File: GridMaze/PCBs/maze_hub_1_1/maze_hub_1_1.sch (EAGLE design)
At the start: 29 parts, among them IC1 7805DT, IC2 TBD62083, IC3 PCA9517D, IC4 PCA9517D, IC5 MCP4541-104E/MS, IC6 OPA197

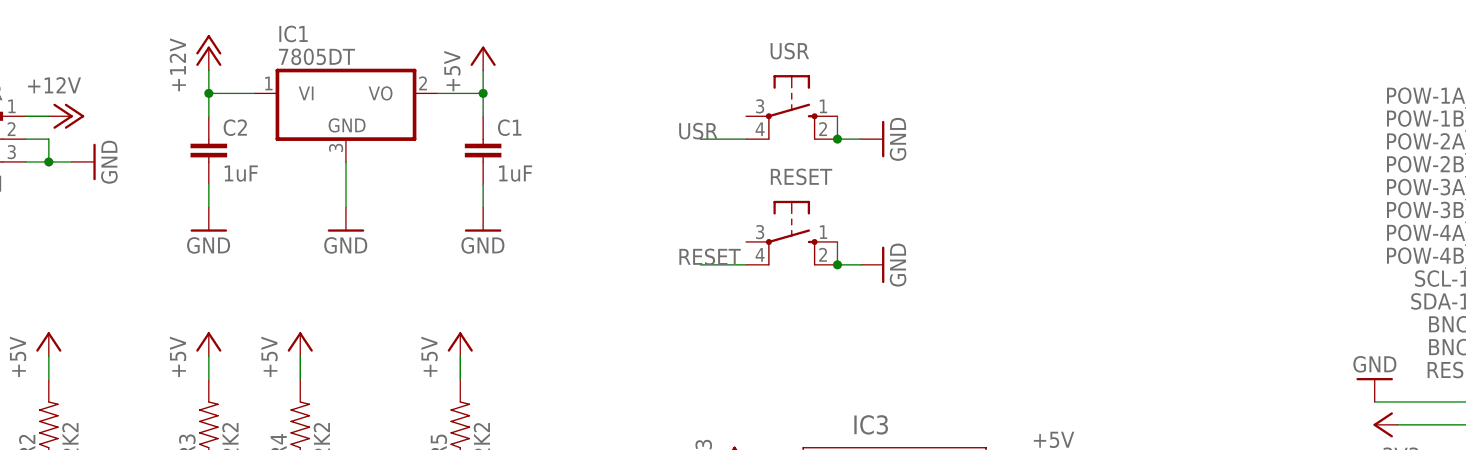
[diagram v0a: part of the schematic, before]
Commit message: Changes to 3x3 GridMaze hardware:
- Rather than seperate tall and short variants there is now a single intermediate height version of the maze.

- IR illumination is now provided by IR module PCBs which connect to the maze hub board using a Molex Micro-Fit cable and can be daisy chained.

- Reduced Poke IR beam current from 50mA to 40mA.
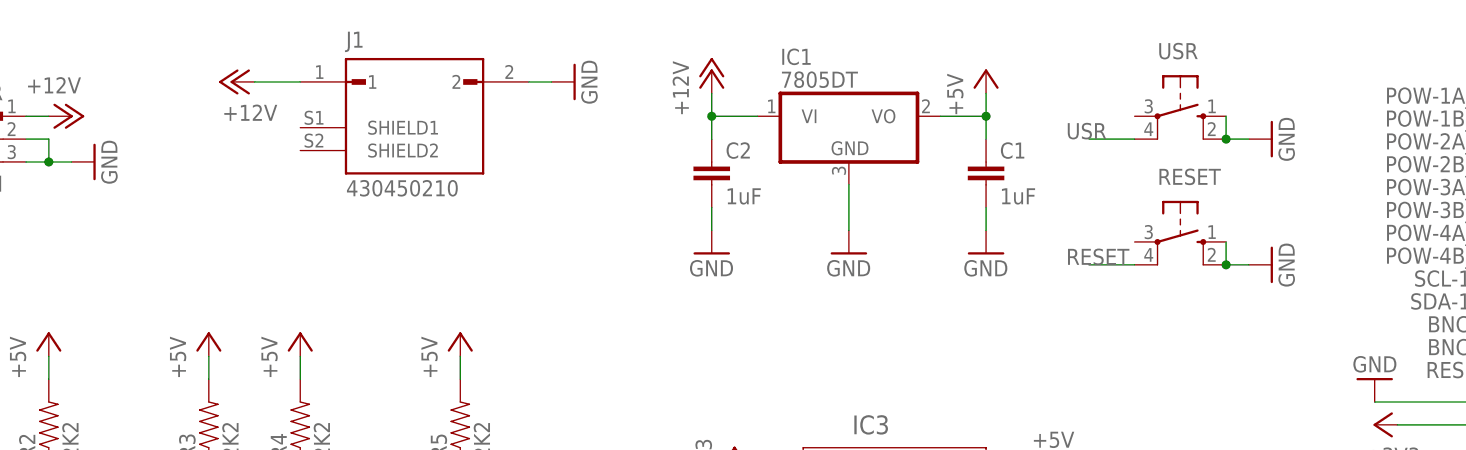
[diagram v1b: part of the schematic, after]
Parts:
- added J1: 430450210, Molex_430450210:430450210
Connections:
- net +12V: now also J1.1
- net GND: now also J1.2
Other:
- moved on the sheet: C1, C2, IC1, RESET, USR
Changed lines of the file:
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@@
 <part name="P+23" library="supply1" deviceset="+5V" device=""/>
 <part name="IC5" library="Digital_potentiometers" deviceset="MCP4541-104E/MS" device=""/>
+<part name="J1" library="Molex_430450210" deviceset="430450210" device=""/>
+<part name="GND13" library="supply1" deviceset="GND" device=""/>
+<part name="P+24" library="supply1" deviceset="+12V" device=""/>
 </parts>
 <sheets>
@@
 </plain>
 <instances>
-<instance part="GND37" gate="1" x="82.55" y="140.97" rot="R90"/>
-<instance part="GND17" gate="1" x="82.55" y="127" rot="R90"/>
+<instance part="GND37" gate="1" x="125.73" y="140.97" rot="R90"/>
+<instance part="GND17" gate="1" x="125.73" y="127" rot="R90"/>
 <instance part="BNC-1" gate="G$1" x="-11.43" y="44.45"/>
 <instance part="BNC-2" gate="G$1" x="-11.43" y="31.75"/>
-<instance part="RESET" gate="1" x="72.39" y="129.54" rot="R270"/>
+<instance part="RESET" gate="1" x="115.57" y="129.54" rot="R270"/>
 <instance part="GND62" gate="1" x="1.27" y="41.91" rot="R90"/>
 <instance part="GND63" gate="1" x="1.27" y="29.21" rot="R90"/>
-<instance part="C1" gate="G$1" x="38.1" y="140.97"/>
-<instance part="C2" gate="G$1" x="7.62" y="140.97"/>
-<instance part="P+2" gate="1" x="7.62" y="151.13"/>
-<instance part="GND2" gate="1" x="7.62" y="130.81"/>
-<instance part="GND3" gate="1" x="22.86" y="130.81"/>
-<instance part="GND4" gate="1" x="38.1" y="130.81"/>
+<instance part="C1" gate="G$1" x="93.98" y="138.43"/>
+<instance part="C2" gate="G$1" x="63.5" y="138.43"/>
+<instance part="P+2" gate="1" x="63.5" y="148.59"/>
+<instance part="GND2" gate="1" x="63.5" y="128.27"/>
+<instance part="GND3" gate="1" x="78.74" y="128.27"/>
+<instance part="GND4" gate="1" x="93.98" y="128.27"/>
 <instance part="GND72" gate="1" x="-10.16" y="63.5" rot="R270"/>
 <instance part="PORT-1" gate="G$1" x="5.08" y="5.08"/>
@@
 <instance part="P+14" gate="1" x="86.36" y="-5.08" rot="R90"/>
 <instance part="P+15" gate="1" x="86.36" y="2.54"/>
-<instance part="P+10" gate="1" x="38.1" y="151.13"/>
+<instance part="P+10" gate="1" x="93.98" y="148.59"/>
 <instance part="POW_CON" gate="G$1" x="-17.78" y="140.97" rot="R180"/>
 <instance part="GND15" gate="1" x="-5.08" y="138.43" rot="R90"/>
@@
 <instance part="GND8" gate="1" x="137.16" y="114.3" rot="R180"/>
 <instance part="FRAME1" gate="G$1" x="-35.56" y="-17.78"/>
-<instance part="USR" gate="1" x="72.39" y="143.51" rot="R270"/>
-<instance part="IC1" gate="A1" x="22.86" y="146.05"/>
+<instance part="USR" gate="1" x="115.57" y="143.51" rot="R270"/>
+<instance part="IC1" gate="A1" x="78.74" y="143.51"/>
 <instance part="SV1" gate="G$1" x="35.56" y="40.64" rot="R180"/>
 <instance part="P+4" gate="1" x="22.86" y="30.48" rot="R90"/>
@@
 <instance part="P+23" gate="1" x="35.56" y="119.38"/>
 <instance part="IC5" gate="G$1" x="134.62" y="43.18"/>
+<instance part="J1" gate="G$1" x="30.48" y="144.78"/>
+<instance part="GND13" gate="1" x="48.26" y="147.32" rot="R90"/>
+<instance part="P+24" gate="1" x="10.16" y="147.32" rot="R90"/>
 </instances>
 <busses>
@@
 <segment>
 <pinref part="P+2" gate="1" pin="+12V"/>
-<wire x1="12.7" y1="146.05" x2="7.62" y2="146.05" width="0.1524" layer="91"/>
-<wire x1="7.62" y1="146.05" x2="7.62" y2="148.59" width="0.1524" layer="91"/>
+<wire x1="68.58" y1="143.51" x2="63.5" y2="143.51" width="0.1524" layer="91"/>
+<wire x1="63.5" y1="143.51" x2="63.5" y2="146.05" width="0.1524" layer="91"/>
 <pinref part="C2" gate="G$1" pin="1"/>
-<wire x1="7.62" y1="143.51" x2="7.62" y2="146.05" width="0.1524" layer="91"/>
-<junction x="7.62" y="146.05"/>
+<wire x1="63.5" y1="140.97" x2="63.5" y2="143.51" width="0.1524" layer="91"/>
+<junction x="63.5" y="143.51"/>
 <pinref part="IC1" gate="A1" pin="VI"/>
 </segment>
@@
 <wire x1="27.178" y1="61.722" x2="22.86" y2="66.04" width="0.1524" layer="91"/>
 </segment>
+<segment>
+<pinref part="J1" gate="G$1" pin="1"/>
+<pinref part="P+24" gate="1" pin="+12V"/>
+<wire x1="12.7" y1="147.32" x2="17.78" y2="147.32" width="0.1524" layer="91"/>
+</segment>
 </net>
 <net name="GND" class="0">
 <segment>
 <pinref part="GND37" gate="1" pin="GND"/>
-<wire x1="77.47" y1="140.97" x2="80.01" y2="140.97" width="0.1524" layer="91"/>
-<wire x1="77.47" y1="143.51" x2="77.47" y2="140.97" width="0.1524" layer="91"/>
+<wire x1="120.65" y1="140.97" x2="123.19" y2="140.97" width="0.1524" layer="91"/>
+<wire x1="120.65" y1="143.51" x2="120.65" y2="140.97" width="0.1524" layer="91"/>
 <pinref part="USR" gate="1" pin="S"/>
 <pinref part="USR" gate="1" pin="S1"/>
-<junction x="77.47" y="140.97"/>
+<junction x="120.65" y="140.97"/>
 </segment>
 <segment>
 <pinref part="GND17" gate="1" pin="GND"/>
-<wire x1="77.47" y1="127" x2="80.01" y2="127" width="0.1524" layer="91"/>
+<wire x1="120.65" y1="127" x2="123.19" y2="127" width="0.1524" layer="91"/>
 <pinref part="RESET" gate="1" pin="S1"/>
 <pinref part="RESET" gate="1" pin="S"/>
-<wire x1="77.47" y1="129.54" x2="77.47" y2="127" width="0.1524" layer="91"/>
-<junction x="77.47" y="127"/>
+<wire x1="120.65" y1="129.54" x2="120.65" y2="127" width="0.1524" layer="91"/>
+<junction x="120.65" y="127"/>
 </segment>
 <segment>
@@
 <segment>
 <pinref part="GND3" gate="1" pin="GND"/>
-<wire x1="22.86" y1="133.35" x2="22.86" y2="138.43" width="0.1524" layer="91"/>
+<wire x1="78.74" y1="130.81" x2="78.74" y2="135.89" width="0.1524" layer="91"/>
 <pinref part="IC1" gate="A1" pin="GND"/>
 </segment>
@@
 <pinref part="C1" gate="G$1" pin="2"/>
 <pinref part="GND4" gate="1" pin="GND"/>
-<wire x1="38.1" y1="133.35" x2="38.1" y2="135.89" width="0.1524" layer="91"/>
+<wire x1="93.98" y1="130.81" x2="93.98" y2="133.35" width="0.1524" layer="91"/>
 </segment>
 <segment>
@@
 <pinref part="C2" gate="G$1" pin="2"/>
 <pinref part="GND2" gate="1" pin="GND"/>
-<wire x1="7.62" y1="135.89" x2="7.62" y2="133.35" width="0.1524" layer="91"/>
+<wire x1="63.5" y1="133.35" x2="63.5" y2="130.81" width="0.1524" layer="91"/>
 </segment>
 <segment>
@@
 <wire x1="66.04" y1="71.12" x2="68.58" y2="71.12" width="0.1524" layer="91"/>
 </segment>
+<segment>
+<pinref part="J1" gate="G$1" pin="2"/>
+<pinref part="GND13" gate="1" pin="GND"/>
+<wire x1="45.72" y1="147.32" x2="43.18" y2="147.32" width="0.1524" layer="91"/>
+</segment>
 </net>
 <net name="RESET" class="0">
 <segment>
-<wire x1="67.31" y1="127" x2="62.23" y2="127" width="0.1524" layer="91"/>
-<label x="59.69" y="127" size="1.778" layer="95"/>
+<wire x1="110.49" y1="127" x2="105.41" y2="127" width="0.1524" layer="91"/>
+<label x="102.87" y="127" size="1.778" layer="95"/>
 <pinref part="RESET" gate="1" pin="P1"/>
 </segment>
@@
 <segment>
 <pinref part="C1" gate="G$1" pin="1"/>
-<wire x1="38.1" y1="143.51" x2="38.1" y2="146.05" width="0.1524" layer="91"/>
-<wire x1="38.1" y1="146.05" x2="33.02" y2="146.05" width="0.1524" layer="91"/>
-<junction x="38.1" y="146.05"/>
-<wire x1="38.1" y1="146.05" x2="38.1" y2="148.59" width="0.1524" layer="91"/>
+<wire x1="93.98" y1="140.97" x2="93.98" y2="143.51" width="0.1524" layer="91"/>
+<wire x1="93.98" y1="143.51" x2="88.9" y2="143.51" width="0.1524" layer="91"/>
+<junction x="93.98" y="143.51"/>
+<wire x1="93.98" y1="143.51" x2="93.98" y2="146.05" width="0.1524" layer="91"/>
 <pinref part="P+10" gate="1" pin="+5V"/>
 <pinref part="IC1" gate="A1" pin="VO"/>
@@
 <net name="USR" class="0">
 <segment>
-<wire x1="67.31" y1="140.97" x2="62.23" y2="140.97" width="0.1524" layer="91"/>
-<label x="59.69" y="140.97" size="1.778" layer="95"/>
+<wire x1="110.49" y1="140.97" x2="105.41" y2="140.97" width="0.1524" layer="91"/>
+<label x="102.87" y="140.97" size="1.778" layer="95"/>
 <pinref part="USR" gate="1" pin="P1"/>
 </segment>
